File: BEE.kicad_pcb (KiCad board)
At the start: 2 copper layers, 73 x 38 mm, 30 parts, among them J1 RPI1_header, J10 Conn_01x02, J11 Conn_01x02, J12 Conn_01x02, J2 BEE_header, J3 Conn_01x03, J4 Conn_01x06, J5 Conn_01x03, J6 Conn_01x05, J7 Conn_01x03, J8 Conn_01x08, J9 Conn_01x02, SW1 SW_Push, SW2 SW_Push, SW3 SW_Push, U1 MCP3008, U2 MCP4911

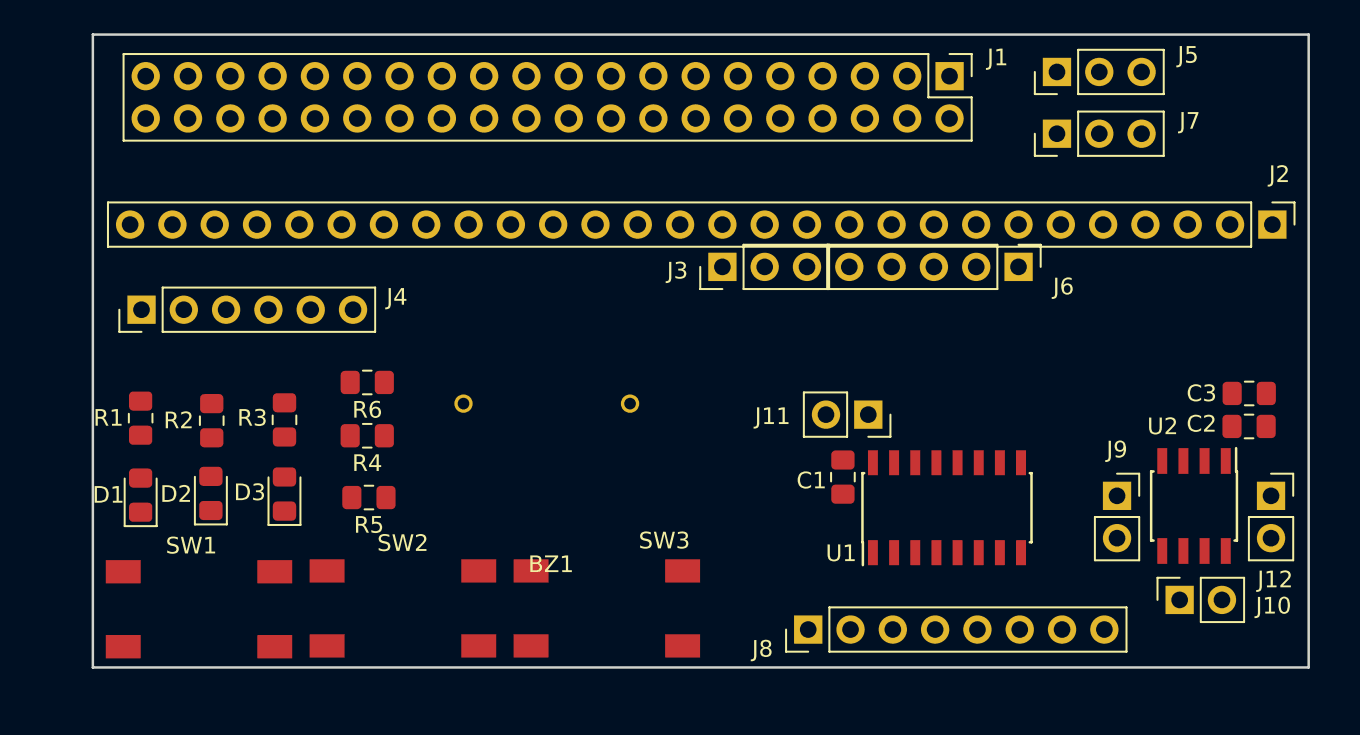
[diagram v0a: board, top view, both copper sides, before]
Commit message: no signal reorder
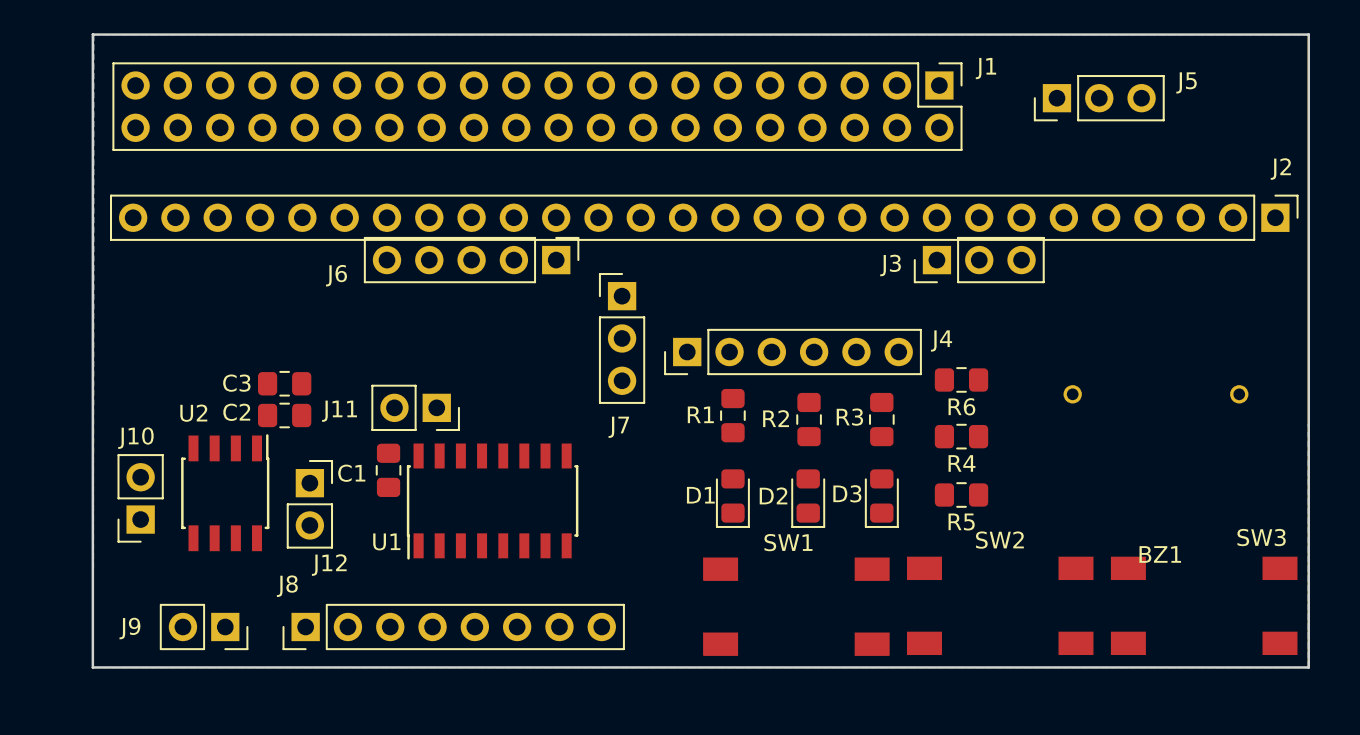
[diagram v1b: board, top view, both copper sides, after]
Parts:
- moved J10 62.6 mm to (102.9, 109.1), turned to 180 degrees
- moved U2 58.2 mm to (108.0, 107.5)
- moved C3 57.9 mm to (111.5, 101.0)
- moved C2 57.9 mm to (111.5, 102.9)
- moved J12 57.7 mm to (113.0, 106.9)
- moved J9 54.1 mm to (108.0, 115.6), turned to 270 degrees
- moved BZ1 36.6 mm to (163.8, 101.6)
- moved D2 35.9 mm to (143.0, 107.7)
- moved SW1 35.9 mm to (142.2, 114.4)
- moved SW2 35.9 mm to (154.5, 114.3)
- moved SW3 35.9 mm to (166.7, 114.3)
- moved D3 35.9 mm to (147.4, 107.7)
- moved R2 35.9 mm to (143.0, 103.1)
- moved R3 35.9 mm to (147.4, 103.1)
- moved R6 35.7 mm to (152.2, 100.7)
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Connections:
- C1 pad 2: GNDA -> GND
- C2 pad 2: GNDA -> GND
- C3 pad 2: GNDA -> GND
- J1 pad 6: GNDA -> GND
- J12 pad 1: GNDA -> GND
- J2 pad 1: /BCM0 -> /BCM2_SDA
- J2 pad 10: /BCM10_MOSI -> /BCM24_TDO
- J2 pad 11: /BCM11_SCLK -> /BCM25_TCK
- J2 pad 12: /BCM12 -> /BCM4_TDI
- J2 pad 13: /BCM13 -> /BCM0
- J2 pad 14: /BCM14_TX -> /BCM1
- J2 pad 15: /BCM15_RX -> /BCM5
- J2 pad 16: /BCM16 -> /BCM6
- J2 pad 17: /BCM17 -> /BCM12
- J2 pad 18: /BCM18_PWM -> /BCM8_CE0
- J2 pad 19: /BCM19 -> /BCM10_MOSI
- J2 pad 2: /BCM1 -> /BCM3_SCL
- J2 pad 20: /BCM20 -> /BCM9_MISO
- J2 pad 21: /BCM21 -> /BCM11_SCLK
- J2 pad 22: /BCM23 -> /BCM7_CE1
- J2 pad 23: /BCM26 -> /BCM13
- J2 pad 24: /BCM22_TRST -> /BCM19
- J2 pad 25: /BCM4_TDI -> /BCM16
- J2 pad 26: /BCM27_TMS -> /BCM20
- J2 pad 27: /BCM25_TCK -> /BCM26
- J2 pad 28: /BCM24_TDO -> /BCM21
- J2 pad 3: /BCM2_SDA -> /BCM14_TX
- J2 pad 4: /BCM3_SCL -> /BCM15_RX
- J2 pad 5: /BCM5 -> /BCM17
- J2 pad 6: /BCM6 -> /BCM23
- J2 pad 7: /BCM7_CE1 -> /BCM18_PWM
- J2 pad 8: /BCM8_CE0 -> /BCM27_TMS
- J2 pad 9: /BCM9_MISO -> /BCM22_TRST
- J6 pad 1: /CE_DAC -> /CE_ADC
- J6 pad 2: /CE_ADC -> /MOSI
- J6 pad 4: /MOSI -> /SCLK
- J6 pad 5: /SCLK -> /CE_DAC
- U1 pad 14: GNDA -> GND
- U1 pad 9: GNDA -> GND
- U2 pad 7: GNDA -> GND
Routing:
- added copper zone on B.Cu, net GND
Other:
- net class Power added: clearance 0.2, trace_width 0.4572, via_dia 0.8, via_drill 0.4
- rule pad_to_mask_clearance: 0.051 -> 0.0508
- rule solder_mask_min_width: 0.25 -> 0.101
- rule trace_min: 0.2 -> 0.1524
- rule via_min_drill: 0.3 -> 0.254
- rule via_min_size: 0.4 -> 0.508

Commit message: small change
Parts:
- moved J2 1.27 mm to (171.0, 92.3)
- moved J3 1.27 mm to (150.7, 94.8)
- moved J6 1.27 mm to (127.8, 94.8)
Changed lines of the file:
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@@
     (last_trace_width 0.3048)
     (user_trace_width 0.1524)
+    (user_trace_width 0.2032)
     (user_trace_width 0.3048)
-    (user_trace_width 0.4572)
+    (user_trace_width 0.4064)
     (trace_clearance 0.2)
     (zone_clearance 0.508)
@@
   )
   (module Connector_PinHeader_2.54mm:PinHeader_1x28_P2.54mm_Vertical (layer F.Cu)
-    (at 171 91 270)
+    (at 171 92.27 270)
     (descr "Through hole straight pin header, 1x28, 2.54mm pitch, single row")
     (tags "Through hole pin header THT 1x28 2.54mm single row")
@@
   )
   (module Connector_PinHeader_2.54mm:PinHeader_1x03_P2.54mm_Vertical (layer F.Cu)
-    (at 150.68 93.54 90)
+    (at 150.68 94.81 90)
     (descr "Through hole straight pin header, 1x03, 2.54mm pitch, single row")
     (tags "Through hole pin header THT 1x03 2.54mm single row")
@@
   )
   (module Connector_PinHeader_2.54mm:PinHeader_1x05_P2.54mm_Vertical (layer F.Cu)
-    (at 127.82 93.54 270)
+    (at 127.82 94.81 270)
     (descr "Through hole straight pin header, 1x05, 2.54mm pitch, single row")
     (tags "Through hole pin header THT 1x05 2.54mm single row")

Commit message: wip: some traces added
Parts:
- moved J7 29.7 mm to (103.4, 87.1), turned to 180 degrees
- moved BZ1 21.6 mm to (142.2, 102.2)
- moved J4 19.4 mm to (154.9, 101.6)
- moved R6 18.9 mm to (170.6, 104.8)
- moved R4 18.7 mm to (170.6, 107.3)
- moved R5 18.5 mm to (170.6, 109.9)
- moved R1 17.2 mm to (155.3, 106.0), turned to 0 degrees
- moved R3 17.1 mm to (164.2, 106.0), turned to 0 degrees
- moved R2 17.0 mm to (159.8, 106.0), turned to 0 degrees
- moved D3 16.9 mm to (164.2, 108.6), turned to 0 degrees
- moved D2 16.8 mm to (159.8, 108.6), turned to 0 degrees
- moved D1 16.8 mm to (155.2, 108.6), turned to 0 degrees
- moved J9 12.8 mm to (102.6, 103.9), turned to 0 degrees
- moved J5 12.4 mm to (170.2, 82.5), turned to 0 degrees
- moved J1 8.56 mm to (159.4, 83.1)
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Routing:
- net +3V3: track 0.00 -> 98.0 mm
- net +5V: track 0.00 -> 78.2 mm, vias 0 -> 1
- net VDD: track 0.00 -> 65.9 mm
- net /BCM2_SDA: track 0.00 -> 22.2 mm
- net /BCM23: track 0.00 -> 22.1 mm
- net /BCM3_SCL: track 0.00 -> 21.6 mm
- net /BCM17: track 0.00 -> 19.1 mm
- net /BCM14_TX: track 0.00 -> 17.7 mm
- net /BCM10_MOSI: track 0.00 -> 17.5 mm
- net /BCM15_RX: track 0.00 -> 17.0 mm
- net /BCM22_TRST: track 0.00 -> 16.5 mm
- net /CE_DAC: track 0.00 -> 16.0 mm, vias 0 -> 1
- net /BCM9_MISO: track 0.00 -> 15.8 mm
- net /BCM4_TDI: track 0.00 -> 14.5 mm
- net /BCM25_TCK: track 0.00 -> 14.5 mm
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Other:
- board size 73 x 38 mm -> 74 x 38 mm
- net class Default: clearance 0.2 -> 0.1524; trace_width 0.25 -> 0.1524; via_dia 0.8 -> 0.508; via_drill 0.4 -> 0.254
- net class Power: clearance 0.2 -> 0.254; trace_width 0.4572 -> 0.6096; via_dia 0.8 -> 0.762; via_drill 0.4 -> 0.381
- net class signal added: clearance 0.2032, trace_width 0.2032, via_dia 0.508, via_drill 0.254
- rule trace_clearance: 0.2 -> 0.1524

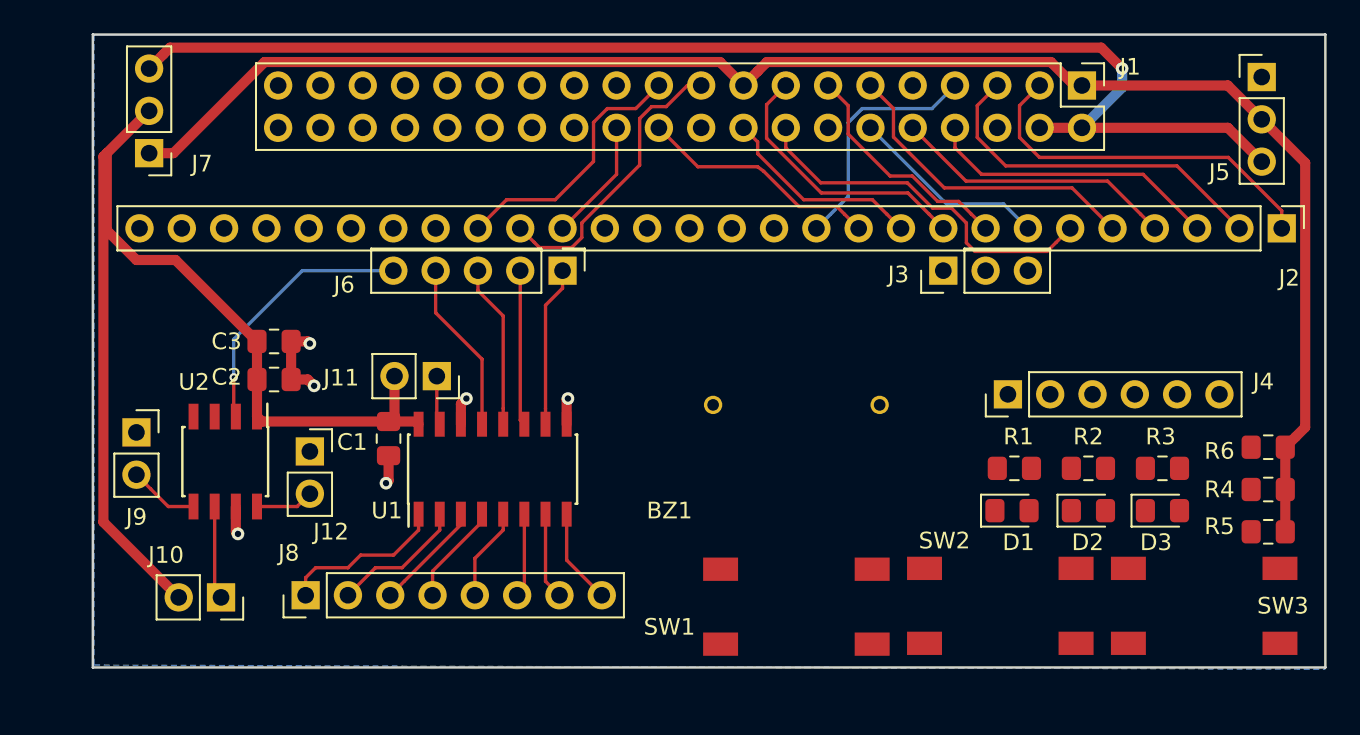
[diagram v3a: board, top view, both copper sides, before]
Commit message: wip:pcb routed, raspi header can be moved right
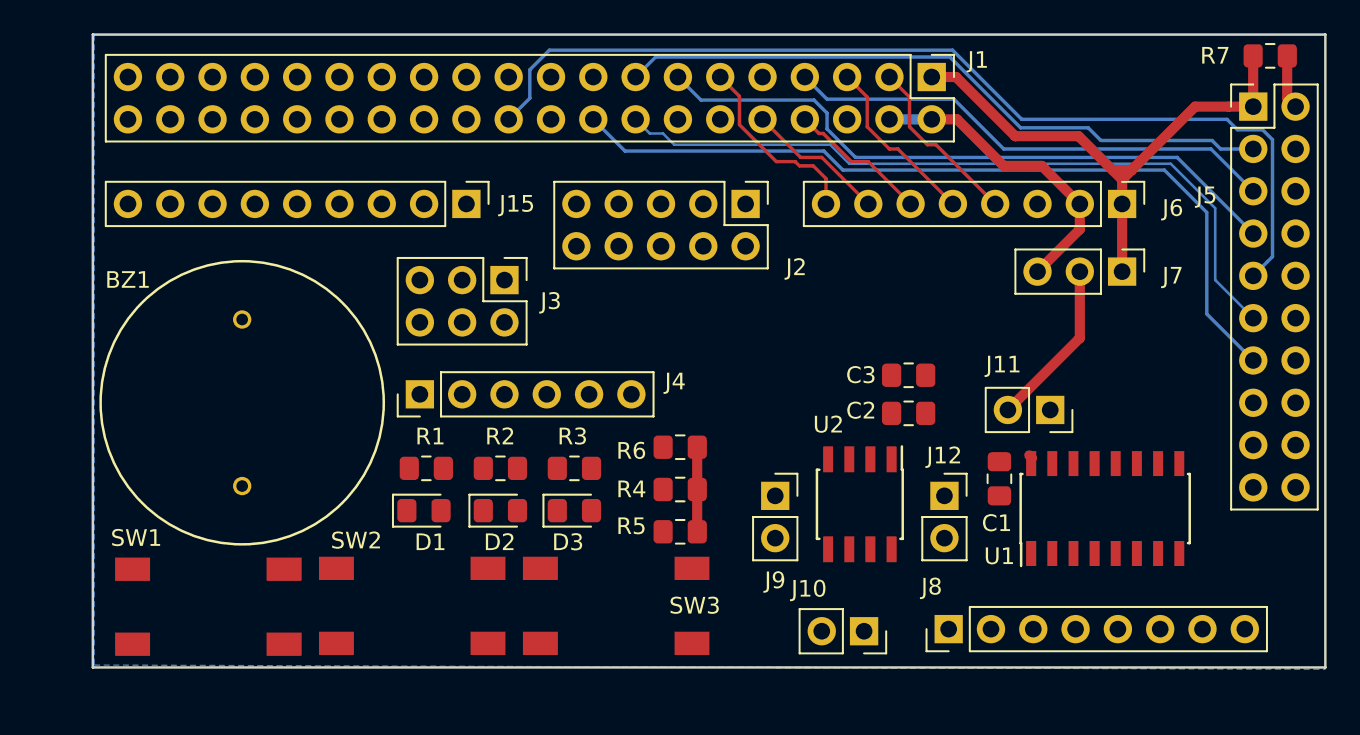
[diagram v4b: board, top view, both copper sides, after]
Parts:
- added J15: Conn_01x09, Connector_PinHeader_2.54mm:PinHeader_1x09_P2.54mm_Vertical, F.Cu at (122.4, 90.2)
- added R7: 0, Resistor_SMD:R_0805_2012Metric_Pad1.15x1.40mm_HandSolder, F.Cu at (170.7, 81.3)
- J2: value BEE_header -> Conn_02x05_Odd_Even; footprint Connector_PinHeader_2.54mm:PinHeader_1x28_P2.54mm_Vertical -> Connector_PinHeader_2.54mm:PinHeader_2x05_P2.54mm_Vertical
- J3: value Conn_01x03 -> Conn_02x03_Odd_Even; footprint Connector_PinHeader_2.54mm:PinHeader_1x03_P2.54mm_Vertical -> Connector_PinHeader_2.54mm:PinHeader_2x03_P2.54mm_Vertical
- J5: value Conn_01x03 -> Conn_02x10_Odd_Even; footprint Connector_PinHeader_2.54mm:PinHeader_1x03_P2.54mm_Vertical -> Connector_PinHeader_2.54mm:PinHeader_2x10_P2.54mm_Vertical
- J6: value Conn_01x05 -> Conn_01x08; footprint Connector_PinHeader_2.54mm:PinHeader_1x05_P2.54mm_Vertical -> Connector_PinHeader_2.54mm:PinHeader_1x08_P2.54mm_Vertical
- moved J7 58.9 mm to (161.8, 94.2), turned to 270 degrees
- moved J10 38.7 mm to (146.3, 115.8)
- moved J8 38.7 mm to (151.4, 115.7)
- moved J9 38.5 mm to (141.0, 107.7)
- moved J12 38.2 mm to (151.1, 107.7)
- moved U2 38.2 mm to (146.1, 108.2)
- moved C2 38.2 mm to (149.0, 102.7)
- moved C3 38.2 mm to (149.0, 100.5)
- moved J11 36.9 mm to (157.5, 102.5)
- moved U1 36.9 mm to (160.8, 108.5)
- moved C1 36.8 mm to (154.4, 106.7)
- moved D2 35.3 mm to (124.5, 108.6)
- moved D3 35.3 mm to (128.9, 108.6)
- moved R1 35.3 mm to (120.0, 106.0)
- moved R2 35.3 mm to (124.5, 106.0)
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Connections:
- J1 pad 12: /BCM18_PWM -> /BCM18_PWM0
- J1 pad 16: /BCM23 -> /BCM23_RTCK
- J1 pad 32: /BCM12 -> /BCM12_PWM0
- J1 pad 33: /BCM13 -> /BCM13_PWM1
- J2 pad 1: /BCM2_SDA -> /BCM8_CE0
- J2 pad 10: /BCM24_TDO -> /CE_DAC
- J2 pad 2: /BCM3_SCL -> /CE_ADC
- J2 pad 3: /BCM14_TX -> /BCM10_MOSI
- J2 pad 4: /BCM15_RX -> /MOSI
- J2 pad 5: /BCM17 -> /BCM9_MISO
- J2 pad 6: /BCM23 -> /MISO
- J2 pad 7: /BCM18_PWM -> /BCM11_SCLK
- J2 pad 8: /BCM27_TMS -> /SCLK
- J2 pad 9: /BCM22_TRST -> /BCM7_CE1
- J3 pad 1: GND -> /BCM18_PWM0
- J3 pad 2: Net-(BZ1-Pad2) -> GND
- J3 pad 3: Net-(BZ1-Pad1) -> /BCM12_PWM0
- J5 pad 1: GND -> +3V3
- J5 pad 2: +3V3 -> Net-(J5-Pad2)
- J5 pad 3: +5V -> /BCM22_TRST
- J6 pad 1: /CE_ADC -> +3V3
- J6 pad 2: /MOSI -> +5V
- J6 pad 3: /MISO -> GND
- J6 pad 4: /SCLK -> /BCM2_SDA
- J6 pad 5: /CE_DAC -> /BCM3_SCL
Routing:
- net +5V: track 78.2 -> 18.7 mm, vias 1 -> 0
- net +3V3: track 98.0 -> 38.5 mm
- net VDD: track 65.9 -> 10.3 mm
- net /BCM25_TCK: track 14.5 -> 59.5 mm
- net /BCM23_RTCK: track 0.00 -> 44.6 mm
- net /BCM24_TDO: track 12.4 -> 49.2 mm
- net /BCM27_TMS: track 14.0 -> 39.0 mm
- net /BCM22_TRST: track 16.5 -> 39.9 mm
- net /BCM23: track 22.1 -> 0.00 mm
- net /BCM10_MOSI: track 17.5 -> 0.00 mm
- net /CE_DAC: track 16.0 -> 0.00 mm, vias 1 -> 0
- net /BCM9_MISO: track 15.8 -> 0.00 mm
- net /BCM4_TDI: track 14.5 -> 29.8 mm
- net /BCM18_PWM: track 12.0 -> 0.00 mm
- net /BCM2_SDA: track 22.2 -> 10.6 mm
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
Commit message: wip: routed, raspi header can be moved right
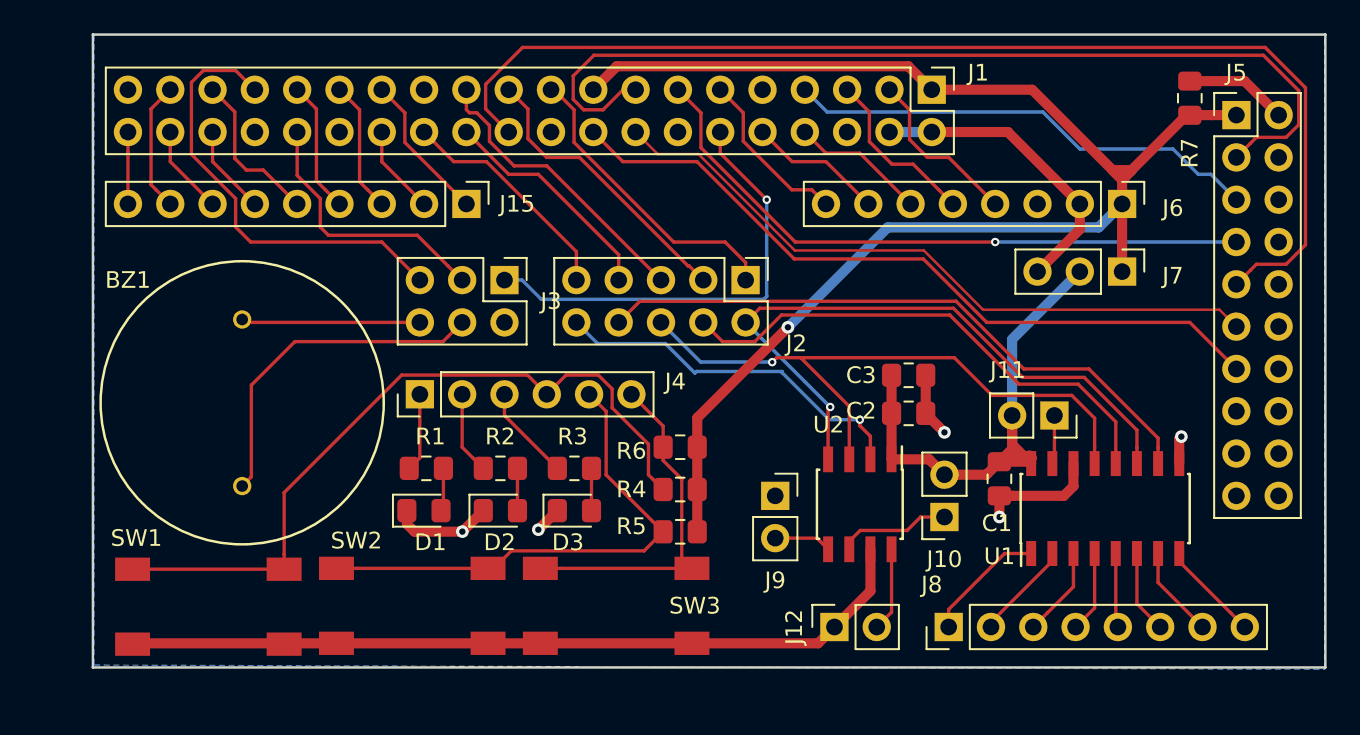
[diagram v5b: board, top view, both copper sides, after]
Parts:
- moved J12 10.3 mm to (144.5, 115.6), turned to 90 degrees
- moved J10 8.39 mm to (151.1, 109.0), turned to 180 degrees
- moved R7 5.45 mm to (165.9, 83.8), turned to 90 degrees
- moved J2 4.57 mm to (139.2, 94.7)
- moved J5 1.14 mm to (168.7, 84.8)
- moved J1 0.76 mm to (150.4, 83.3)
- moved J11 0.42 mm to (157.7, 102.9)
- moved J8 0.13 mm to (151.4, 115.6)
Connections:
- J2 pad 1: /BCM8_CE0 -> /BCM10_MOSI
- J2 pad 2: /CE_ADC -> /MOSI
- J2 pad 3: /BCM10_MOSI -> /BCM9_MISO
- J2 pad 4: /MOSI -> /MISO
- J2 pad 5: /BCM9_MISO -> /BCM11_SCLK
- J2 pad 6: /MISO -> /SCLK
- J2 pad 7: /BCM11_SCLK -> /BCM8_CE0
- J2 pad 8: /SCLK -> /CE_ADC
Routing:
- net GND: track 0.00 -> 68.7 mm, vias 0 -> 5
- net +3V3: track 38.5 -> 89.6 mm, vias 0 -> 1
- net /SW3: track 0.00 -> 44.9 mm
- net /MOSI: track 0.00 -> 39.3 mm, vias 0 -> 1
- net /SCLK: track 0.00 -> 38.7 mm, vias 0 -> 1
- net /CE_ADC: track 0.00 -> 37.8 mm
- net /MISO: track 0.00 -> 31.1 mm
- net /SW2: track 0.00 -> 30.6 mm
- net /BCM18_PWM0: track 0.00 -> 27.3 mm, vias 0 -> 1
- net /BCM13_PWM1: track 0.00 -> 26.7 mm
- net /CE_DAC: track 0.00 -> 22.2 mm, vias 0 -> 1
- net VDD: track 10.3 -> 32.0 mm
- net /SW1: track 0.00 -> 21.1 mm
- net Net-(BZ1-Pad1): track 0.00 -> 20.5 mm
- net /BCM10_MOSI: track 0.00 -> 18.2 mm
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
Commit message: wip some traces re-routed
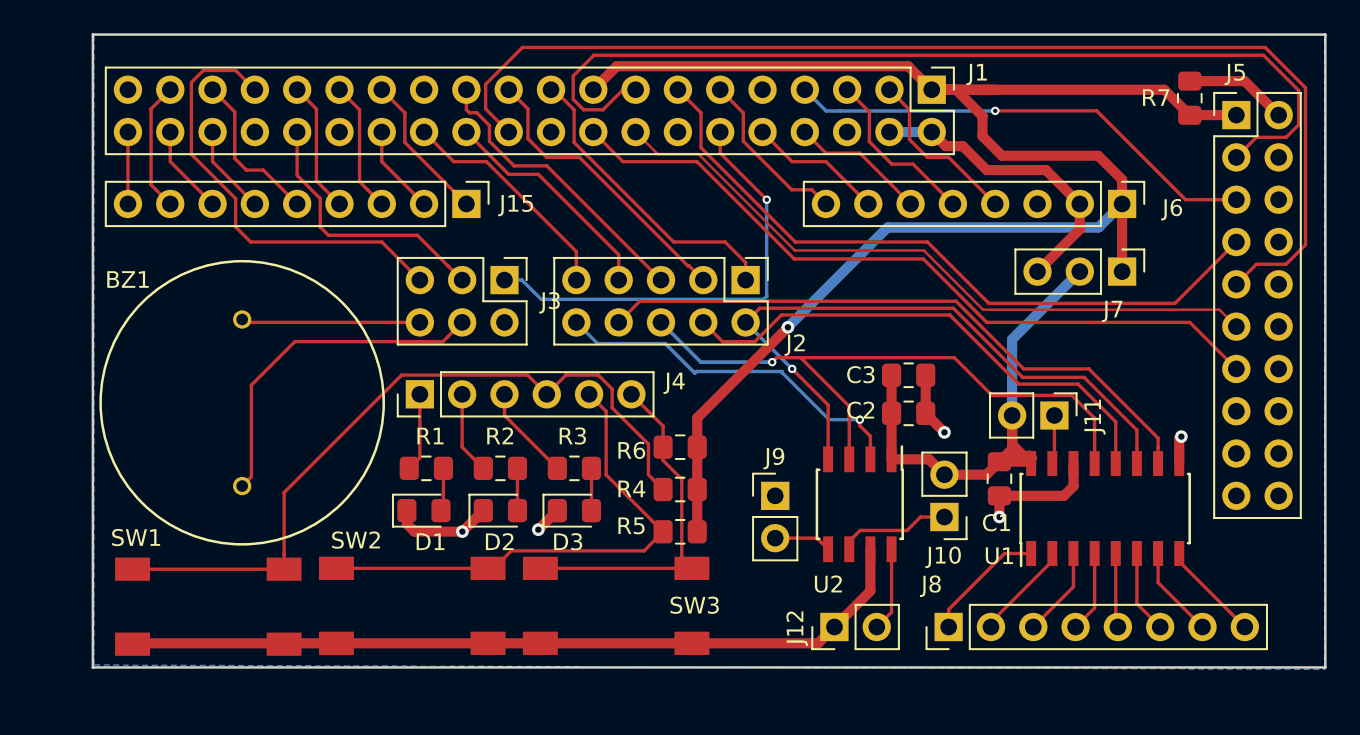
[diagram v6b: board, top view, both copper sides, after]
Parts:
- J10, J11, J12, J9: footprint Connector_PinSocket_2.54mm:PinSocket_1x02_P2.54mm_Vertical -> Connector_PinHeader_2.54mm:PinHeader_1x02_P2.54mm_Vertical
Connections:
- J5 pad 15: (no net) -> Net-(J5-Pad15)
- J5 pad 17: (no net) -> Net-(J5-Pad17)
- J5 pad 19: (no net) -> Net-(J5-Pad19)
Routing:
- net +3V3: track 89.6 -> 102.0 mm
- net /BCM27_TMS: track 38.5 -> 41.6 mm, vias 1 -> 0
- net /BCM4_TDI: vias 0 -> 1
